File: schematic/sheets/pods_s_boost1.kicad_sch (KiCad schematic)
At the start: 6 parts, among them J1 WATER-1x03

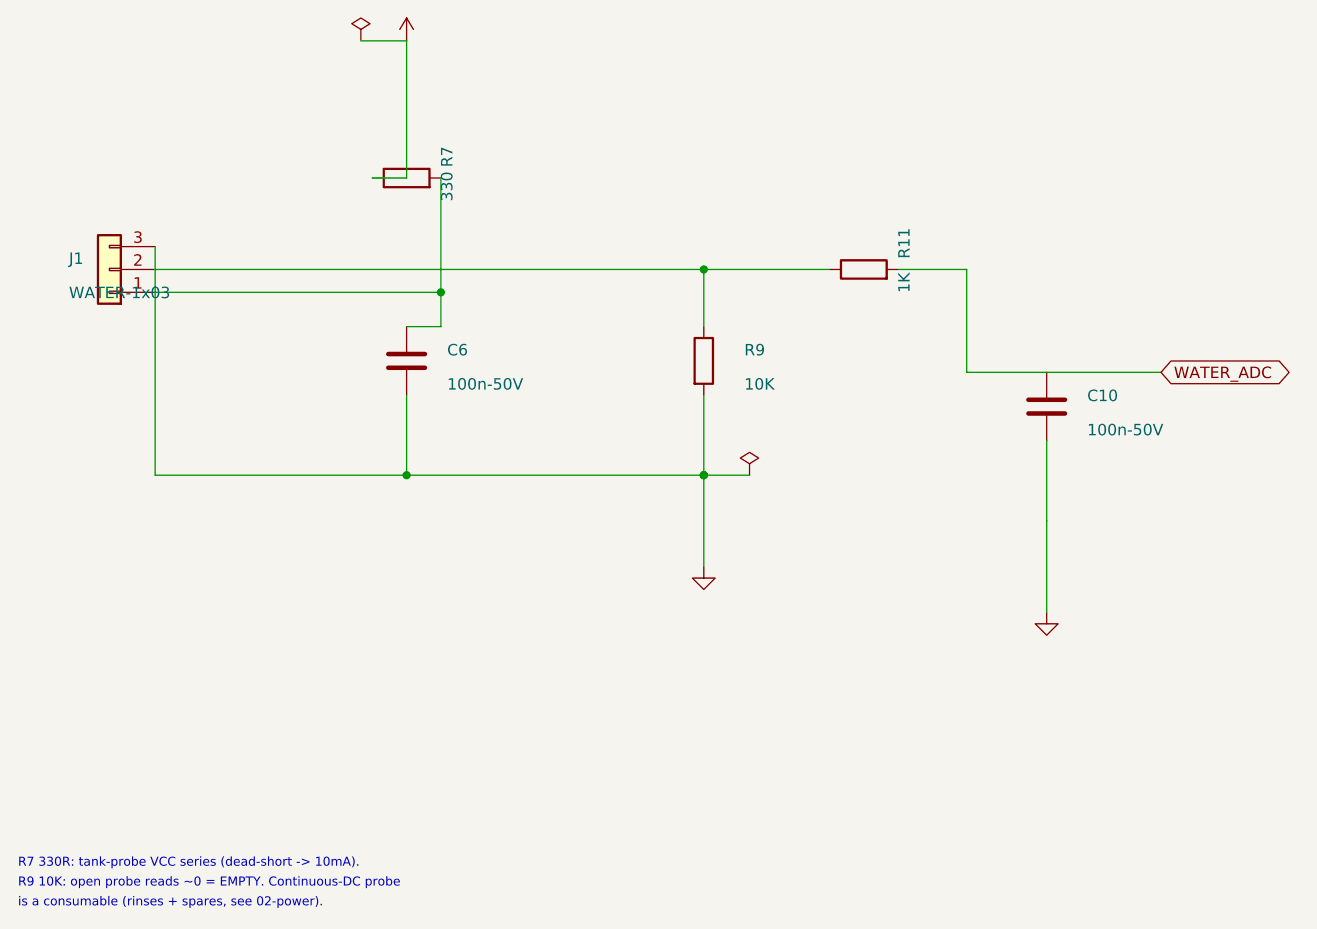
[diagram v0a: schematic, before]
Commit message: Organize schematic/: sheets/ mfg/ final/, drop sklib
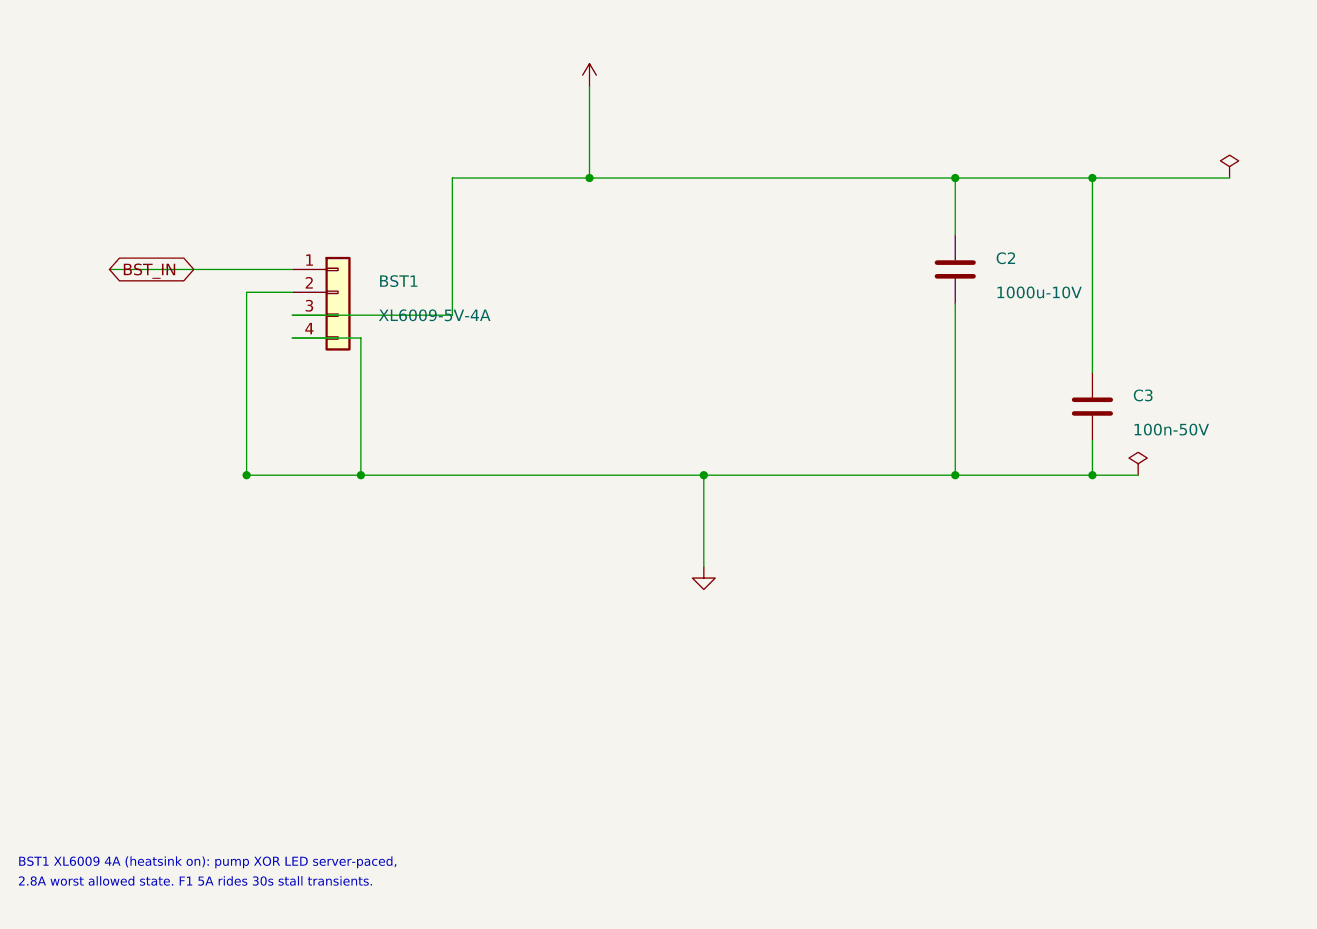
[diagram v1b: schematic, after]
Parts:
- removed C10, C6: 100n-50V, Capacitor_SMD:C_0603_1608Metric, symbol Device:C
- removed J1: WATER-1x03, Connector_PinHeader_2.54mm:PinHeader_1x03_P2.54mm_Vertical, symbol Connector_Generic:Conn_01x03
- removed R11: 1K, Resistor_SMD:R_0603_1608Metric, symbol Device:R
- removed R7: 330, Resistor_SMD:R_0603_1608Metric, symbol Device:R
- removed R9: 10K, Resistor_SMD:R_0603_1608Metric, symbol Device:R
- added BST1: XL6009-5V-4A, Connector_PinHeader_2.54mm:PinHeader_1x04_P2.54mm_Vertical, symbol Connector_Generic:Conn_01x04
- added C2: 1000u-10V, Capacitor_THT:CP_Radial_D8.0mm_P3.50mm, symbol Device:C
- added C3: 100n-50V, Capacitor_SMD:C_0603_1608Metric, symbol Device:C
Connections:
- net GND: now also BST1.2 (Pin_2), BST1.4 (Pin_4), C2.2, C3.2
- new net +5V: BST1.3 (Pin_3), C2.1, C3.1
- new net BST_IN: BST1.1 (Pin_1)
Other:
- note added: "2.8A worst allowed state. F1 5A rides 30s stall transients."
- note added: "BST1 XL6009 4A (heatsink on): pump XOR LED server-paced,"
- note removed: "R7 330R: tank-probe VCC series (dead-short -> 10mA)."
- note removed: "R9 10K: open probe reads ~0 = EMPTY. Continuous-DC probe"
- note removed: "is a consumable (rinses + spares, see 02-power)."
